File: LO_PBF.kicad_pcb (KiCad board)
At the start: 2 copper layers, 171.1 x 60 mm, 10 parts, among them J1 Conn_Coaxial, J2 Conn_Coaxial

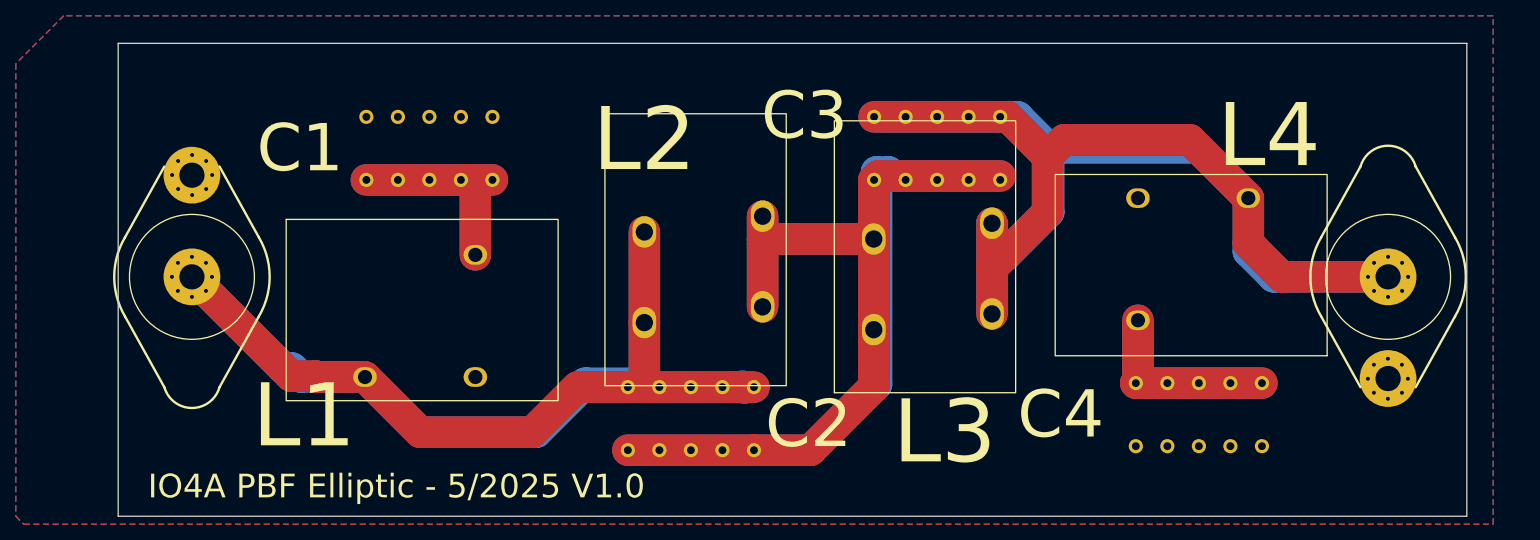
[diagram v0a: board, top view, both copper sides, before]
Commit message: like ordered to JLCPCB
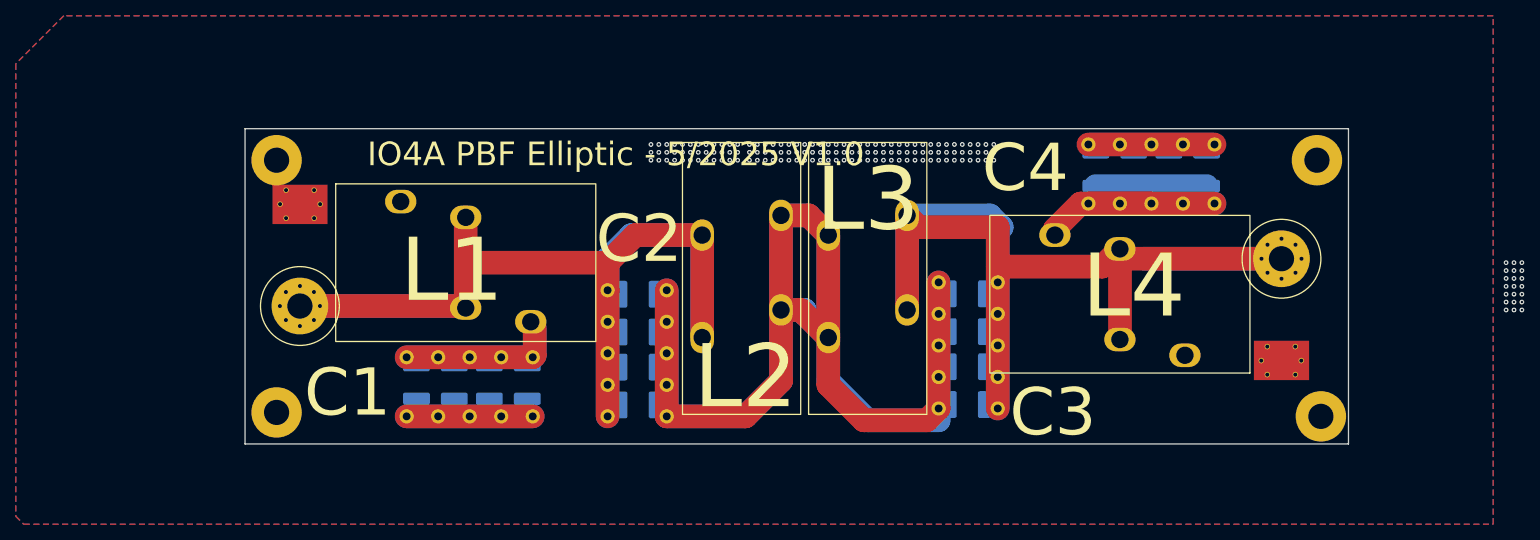
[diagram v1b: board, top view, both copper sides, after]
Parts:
- added C1d1: C, 3_Condensatori:C_1812_multiplo, B.Cu at (168.3, 85.0)
- added C1d2: C, 3_Condensatori:C_1812_multiplo, B.Cu at (210.1, 85.0)
- added C1d3: C, 3_Condensatori:C_1812_multiplo, B.Cu at (233.4, 62.1)
- added C1d4: C, 3_Condensatori:C_1812_multiplo, B.Cu at (147.2, 89.1)
- added H1: MountingHole_Pad, MountingHole:MountingHole_3.2mm_M3_Pad, F.Cu at (122.5, 93.0)
- added H2: MountingHole_Pad, MountingHole:MountingHole_3.2mm_M3_Pad, F.Cu at (122.5, 61.0)
- added H3: MountingHole_Pad, MountingHole:MountingHole_3.2mm_M3_Pad, F.Cu at (254.5, 61.0)
- added H4: MountingHole_Pad, MountingHole:MountingHole_3.2mm_M3_Pad, F.Cu at (255.0, 93.5)
- J1, J2: footprint 2_Connettori:PL-SO-239-2-hole-one-gnd -> 1_Induttori:coax_solder
- moved C4 31.3 mm to (232.5, 63.0), turned to 90 degrees
- moved C1 30.8 mm to (148.0, 89.5), turned to -90 degrees
- moved C3 26.2 mm to (210.5, 85.5), turned to 180 degrees
- moved J1 14.2 mm to (125.5, 79.5)
- moved J2 13.7 mm to (250.0, 73.5)
- moved C2 9.17 mm to (168.5, 86.5), turned to 180 degrees
- moved L2 8.71 mm to (181.5, 76.0)
- moved L4 7.77 mm to (229.5, 78.0)
- moved L3 7.72 mm to (197.5, 76.0)
- moved L1 6.28 mm to (146.5, 74.0)
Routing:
- net Net-(J2-In): track 217.2 -> 161.4 mm
- net GND: track 0.00 -> 48.0 mm, vias 0 -> 153
- net Net-(J1-In): track 206.3 -> 164.3 mm
- net Net-(C1d1-Pad2): track 206.4 -> 239.5 mm
- net Net-(C1d3-Pad2): track 48.2 -> 60.4 mm
- net Net-(C1-Pad1): track 51.6 -> 39.7 mm
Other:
- board size 171.1 x 60 mm -> 140 x 40 mm

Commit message: update
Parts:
- moved L1 2.82 mm to (143.7, 74.3), turned to 180 degrees
- moved L4 1.55 mm to (231.0, 78.4), turned to 0 degrees
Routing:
- net Net-(J1-In): track 164.3 -> 198.0 mm
- net Net-(C1d3-Pad2): track 60.4 -> 83.3 mm
- net Net-(J2-In): track 161.4 -> 183.1 mm
- net Net-(C1-Pad1): track 39.7 -> 53.5 mm
